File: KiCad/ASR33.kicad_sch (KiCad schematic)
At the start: 34 parts, among them J1 USB-C, J2 Start, J3 Control, J4 Tx/Rx, U1 ESP32-WROOM-32, U2 FT231XQ, U3 NCR402U, U4 NCR402U, U5 NX6020CAKS, U6 LMR16006+FB

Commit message: Notes
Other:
- note added: "Look in to clamp diode on Rx Check all GPIO are clean Add QR code"
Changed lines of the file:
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@@
     (stroke (width 0) (type default) (color 0 0 0 0))
+  )
+  (text "Look in to clamp diode on Rx\nCheck all GPIO are clean\nAdd QR code"
+    (at 29.845 127.635 0)
+    (effects (font (size 10 10) (thickness 2) bold) (justify left bottom))
   )
   (global_label "MOTOR" (shape input) (at 127 113.03 180) (fields_autoplaced)

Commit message: Reworked
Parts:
- removed J2: Start, RevK:Molex_MiniSPOX_H2RA, symbol Connector_Generic:Conn_01x02
- removed J3: Control, RevK:Molex_MiniSPOX_H3RA, symbol Connector_Generic:Conn_01x03
- removed J4: Tx/Rx, RevK:Molex_MiniSPOX_H4RA, symbol Connector_Generic:Conn_01x04
- removed R9: 10K, RevK:R_0603, symbol Device:R
- removed U5: NX6020CAKS, Package_TO_SOT_SMD:SOT-363_SC-70-6, symbol RevK:NX6020CAKS
- added C5: NF, RevK:C_0603, symbol Device:C
- added J2: Control, RevK:Molex_MiniSPOX_H3RA, symbol Connector_Generic:Conn_01x03
- added J3: Teletype, RevK:Molex_MiniSPOX_H6RA, symbol Connector_Generic:Conn_01x06
- added Q1: NX7002AK, Package_TO_SOT_SMD:SOT-23, symbol RevK:NX7002AK
- added U6: QR, RevK:QR-ASR33, symbol RevK:QR
- renumbered C5 to C6, C6 to C7, C7 to C8, R11 to R9, U6 to U5
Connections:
- net CHARGER: now also U1.24 (IO2); no longer U1.29 (IO5)
- net GND: now also C5.1, J2.1 (Pin_1), J3.1 (Pin_1), Q1.2 (S)
- net MOTOR: now also D2.6 (K3A4), U1.37 (IO23), J2.3 (Pin_3); no longer D2.3 (K1A2), U1.30 (IO18)
- net POWER: now also D2.3 (K1A2), U1.36 (IO22), J2.2 (Pin_2); no longer D2.6 (K3A4), U1.31 (IO19)
- net RX20MA: now also D3.6 (K3A4), U1.28 (IO17), C5.2, J3.6 (Pin_6); no longer D3.3 (K1A2), U1.27 (IO16)
- net START: now also D3.3 (K1A2), U1.26 (IO4), J3.2 (Pin_2); no longer D3.6 (K3A4), U1.37 (IO23)
- net TX20MA: now also U1.27 (IO16), Q1.1 (G); no longer U1.26 (IO4)
- net USB: now also U1.23 (IO15); no longer U1.28 (IO17)
- net at U3.2 (IOUT), U3.3 (IOUT), U3.5 (IOUT): now also J3.3 (Pin_3)
- net at U4.2 (IOUT), U4.3 (IOUT), U4.5 (IOUT): now also J3.5 (Pin_5)
- new net: J3.4 (Pin_4), Q1.3 (D)
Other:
- note removed: "Look in to clamp diode on Rx Check all GPIO are clean Add QR code"
- moved on the sheet: R9

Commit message: New PCB
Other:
- note added: "Maybe button for AP mode?"
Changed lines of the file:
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@@
     (stroke (width 0) (type default) (color 0 0 0 0))
+  )
+  (text "Maybe button for AP mode?" (at 34.925 23.495 0)
+    (effects (font (size 10 10) (thickness 2) bold) (justify left bottom))
   )
   (global_label "MOTOR" (shape input) (at 127 97.79 180) (fields_autoplaced)

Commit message: Tweak, added button
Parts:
- added SW1: SW_Push, RevK:SW_PUSH_6mm_PTH, symbol Switch:SW_Push
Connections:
- net GND: now also SW1.1
- net BUTTON: now reaches U1.16 (IO13)
- net BUTTON: now also SW1.2
- no-connect marks 25 -> 24
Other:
- note removed: "Maybe button for AP mode?"

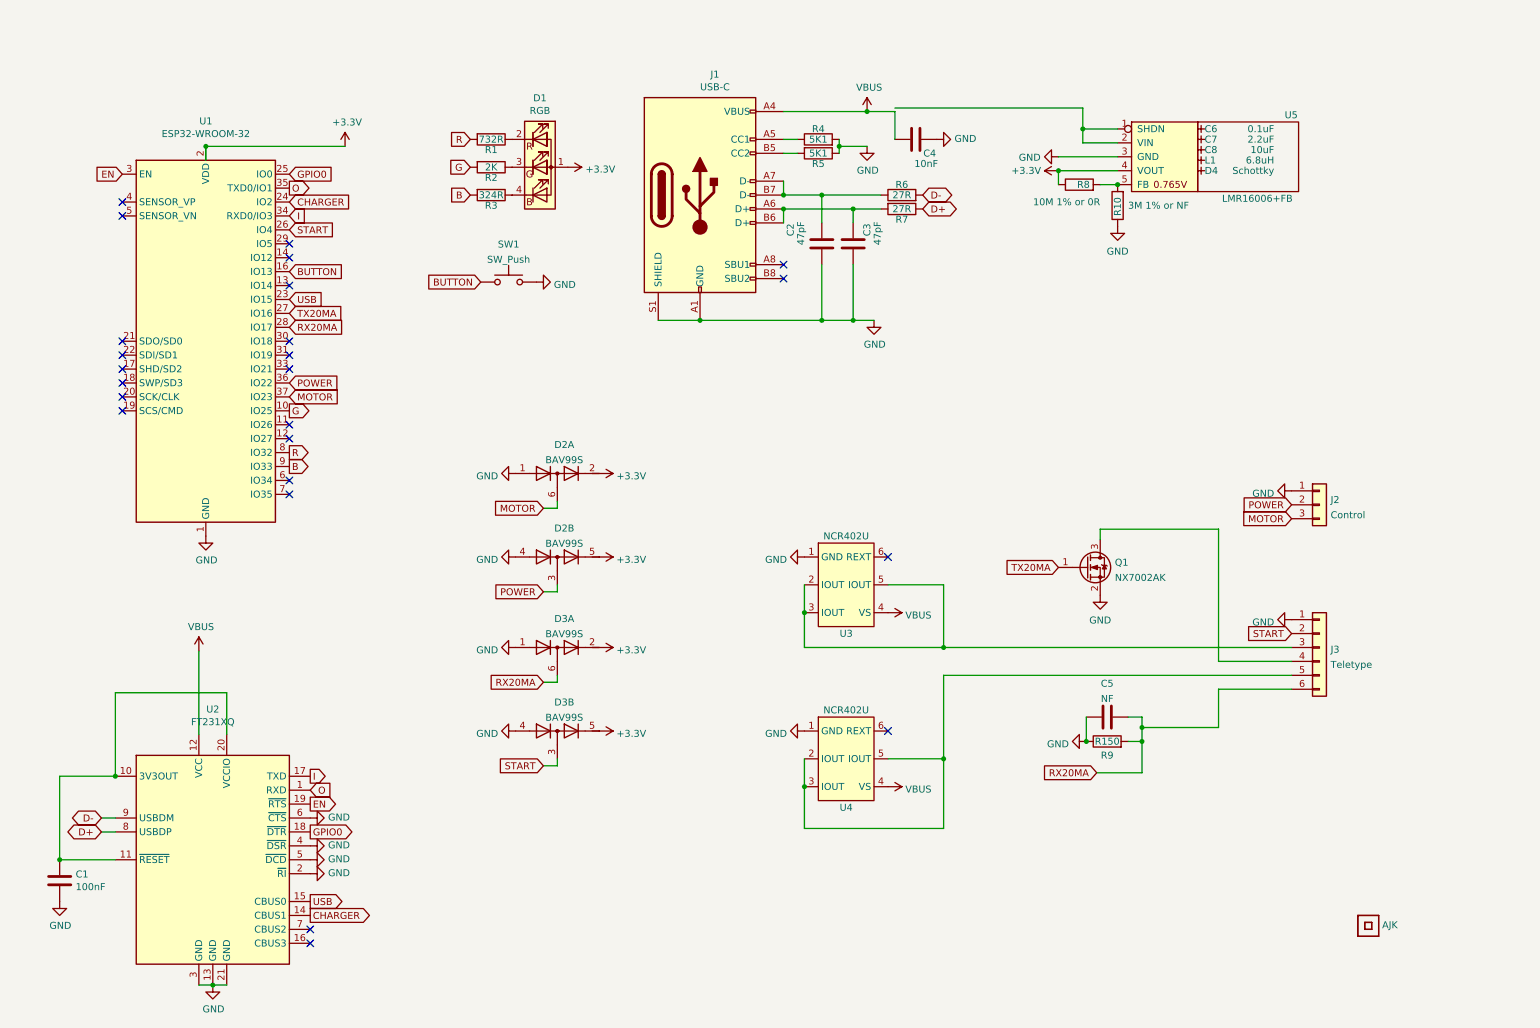
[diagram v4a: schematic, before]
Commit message: Reworkd tx/rx
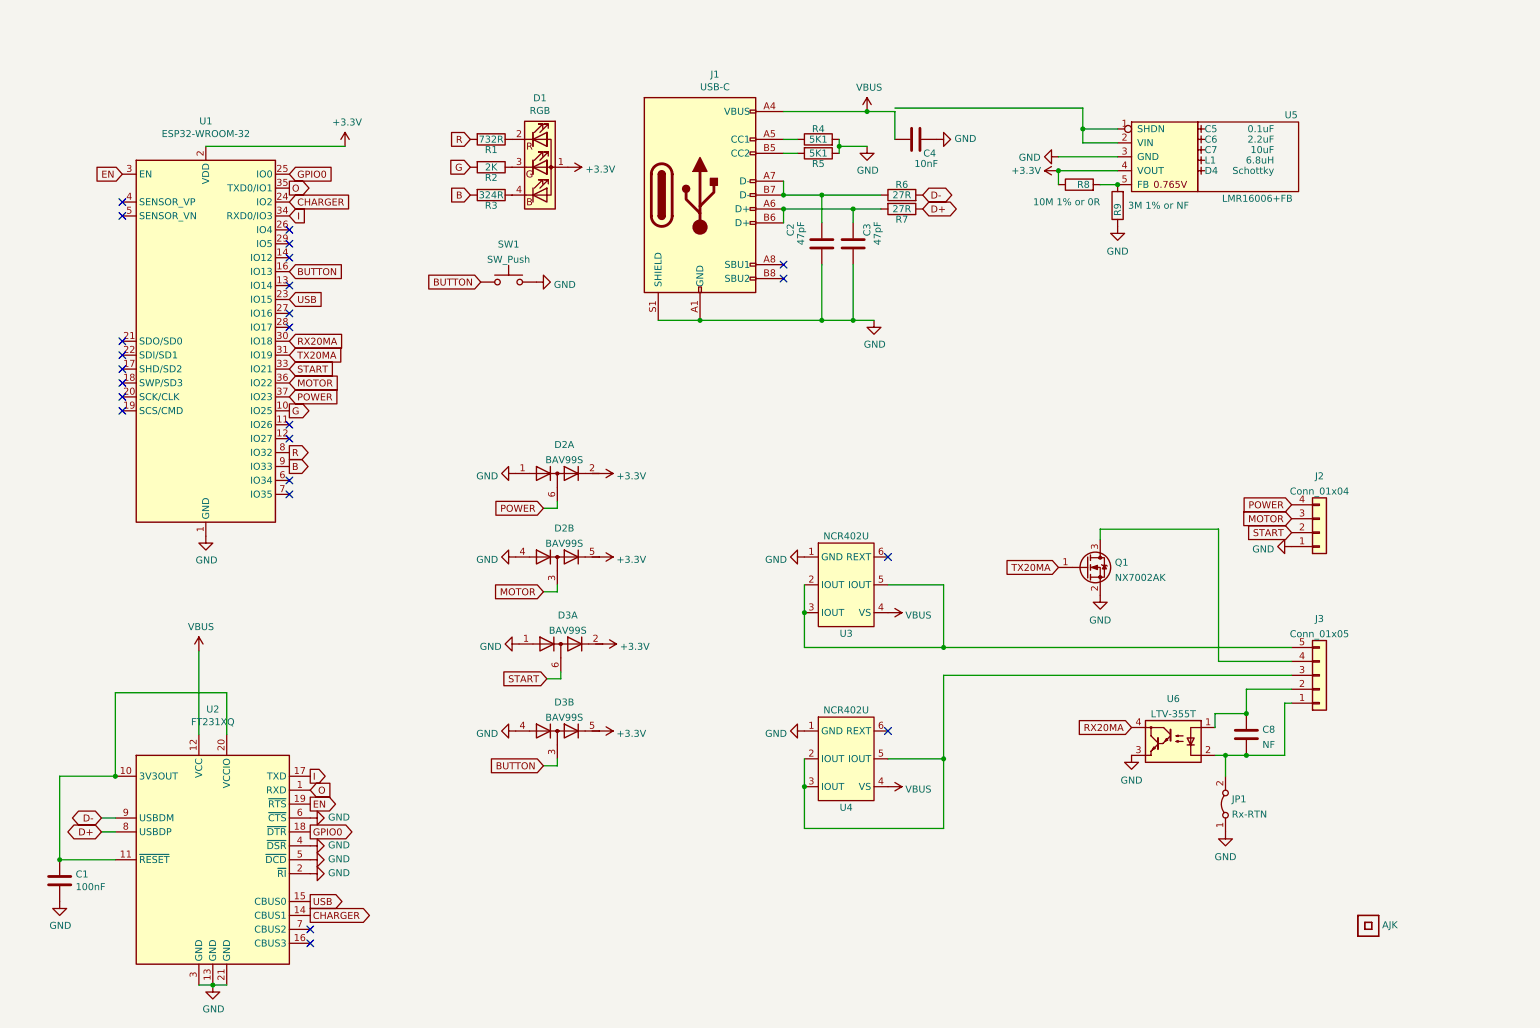
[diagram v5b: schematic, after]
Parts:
- removed J2: Control, RevK:Molex_MiniSPOX_H3RA, symbol Connector_Generic:Conn_01x03
- removed J3: Teletype, RevK:Molex_MiniSPOX_H6RA, symbol Connector_Generic:Conn_01x06
- removed R9: R150, RevK:R_0603, symbol Device:R
- added J2: Conn_01x04, RevK:Molex_MiniSPOX_H4RA, symbol Connector_Generic:Conn_01x04
- added J3: Conn_01x05, RevK:Molex_MiniSPOX_H5RA, symbol Connector_Generic:Conn_01x05
- added JP1: Rx-RTN, Jumper:SolderJumper-2_P1.3mm_Bridged2Bar_RoundedPad1.0x1.5mm, symbol Jumper:Jumper_2_Bridged
- added U6: LTV-355T, Package_SO:SO-4_4.4x3.6mm_P2.54mm, symbol Isolator:LTV-355T
- renumbered C6 to C5, C7 to C6, C8 to C7, C5 to C8, R10 to R9, U6 to U7
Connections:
- net BUTTON: now also D3.3 (K1A2)
- net GND: now also J2.1 (Pin_1), JP1.1 (A), U6.3; no longer C8.1
- net MOTOR: now also D2.3 (K1A2), U1.36 (IO22), J2.3 (Pin_3); no longer D2.6 (K3A4), U1.37 (IO23)
- net POWER: now also D2.6 (K3A4), U1.37 (IO23), J2.4 (Pin_4); no longer D2.3 (K1A2), U1.36 (IO22)
- net RX20MA: now also U1.30 (IO18), U6.4; no longer C8.2, D3.6 (K3A4), U1.28 (IO17)
- net START: now also D3.6 (K3A4), U1.33 (IO21), J2.2 (Pin_2); no longer D3.3 (K1A2), U1.26 (IO4)
- net TX20MA: now also U1.31 (IO19); no longer U1.27 (IO16)
- net at Q1.3 (D): now also J3.4 (Pin_4)
- net at U3.2 (IOUT), U3.3 (IOUT), U3.5 (IOUT): now also J3.5 (Pin_5)
- net at U4.2 (IOUT), U4.3 (IOUT), U4.5 (IOUT): now also J3.3 (Pin_3)
- new net: C8.1, J3.1 (Pin_1), JP1.2 (B), U6.2
- new net: C8.2, J3.2 (Pin_2), U6.1
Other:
- moved on the sheet: C8

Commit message: Reworked PCB and manuals
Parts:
- JP1: footprint Jumper:SolderJumper-2_P1.3mm_Bridged2Bar_RoundedPad1.0x1.5mm -> RevK:SolderJumper-2_P1.3mm_Bridged2Bar_RoundedPad1.0x1.5mm
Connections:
- net MOTOR renamed MTR
- net POWER renamed PWR
- net START renamed RUN
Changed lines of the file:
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@@
     (stroke (width 0) (type default) (color 0 0 0 0))
   )
-  (global_label "MOTOR" (shape input) (at 127 113.03 180) (fields_autoplaced)
+  (global_label "MTR" (shape input) (at 127 113.03 180) (fields_autoplaced)
     (effects (font (size 1.27 1.27)) (justify right))
-    (property "Intersheet References" "${INTERSHEET_REFS}" (id 0) (at 118.3258 112.9506 0)
+    (property "Intersheet References" "${INTERSHEET_REFS}" (id 0) (at 120.9868 112.9506 0)
       (effects (font (size 1.27 1.27)) (justify right) hide)
     )
@@
     )
   )
-  (global_label "START" (shape input) (at 127.635 128.905 180) (fields_autoplaced)
+  (global_label "RUN" (shape input) (at 127.635 128.905 180) (fields_autoplaced)
     (effects (font (size 1.27 1.27)) (justify right))
-    (property "Intersheet References" "${INTERSHEET_REFS}" (id 0) (at 119.8075 128.8256 0)
+    (property "Intersheet References" "${INTERSHEET_REFS}" (id 0) (at 121.3798 128.8256 0)
       (effects (font (size 1.27 1.27)) (justify right) hide)
     )
@@
     )
   )
-  (global_label "START" (shape input) (at 263.525 102.235 180) (fields_autoplaced)
+  (global_label "RUN" (shape input) (at 263.525 102.235 180) (fields_autoplaced)
     (effects (font (size 1.27 1.27)) (justify right))
-    (property "Intersheet References" "${INTERSHEET_REFS}" (id 0) (at 255.6975 102.1556 0)
+    (property "Intersheet References" "${INTERSHEET_REFS}" (id 0) (at 257.2698 102.1556 0)
       (effects (font (size 1.27 1.27)) (justify right) hide)
     )
@@
     )
   )
-  (global_label "POWER" (shape input) (at 263.525 97.155 180) (fields_autoplaced)
+  (global_label "PWR" (shape input) (at 263.525 97.155 180) (fields_autoplaced)
     (effects (font (size 1.27 1.27)) (justify right))
-    (property "Intersheet References" "${INTERSHEET_REFS}" (id 0) (at 254.7298 97.0756 0)
+    (property "Intersheet References" "${INTERSHEET_REFS}" (id 0) (at 257.2094 97.0756 0)
       (effects (font (size 1.27 1.27)) (justify right) hide)
     )
@@
     )
   )
-  (global_label "MOTOR" (shape input) (at 80.645 74.93 0) (fields_autoplaced)
-    (effects (font (size 1.27 1.27)) (justify left))
-    (property "Intersheet References" "${INTERSHEET_REFS}" (id 0) (at 89.3192 74.8506 0)
+  (global_label "MTR" (shape input) (at 80.645 74.93 0) (fields_autoplaced)
+    (effects (font (size 1.27 1.27)) (justify left))
+    (property "Intersheet References" "${INTERSHEET_REFS}" (id 0) (at 86.6582 74.8506 0)
       (effects (font (size 1.27 1.27)) (justify left) hide)
     )
@@
     )
   )
-  (global_label "POWER" (shape input) (at 80.645 77.47 0) (fields_autoplaced)
-    (effects (font (size 1.27 1.27)) (justify left))
-    (property "Intersheet References" "${INTERSHEET_REFS}" (id 0) (at 89.4402 77.3906 0)
+  (global_label "PWR" (shape input) (at 80.645 77.47 0) (fields_autoplaced)
+    (effects (font (size 1.27 1.27)) (justify left))
+    (property "Intersheet References" "${INTERSHEET_REFS}" (id 0) (at 86.9606 77.3906 0)
       (effects (font (size 1.27 1.27)) (justify left) hide)
     )
@@
     )
   )
-  (global_label "POWER" (shape input) (at 127 97.79 180) (fields_autoplaced)
+  (global_label "PWR" (shape input) (at 127 97.79 180) (fields_autoplaced)
     (effects (font (size 1.27 1.27)) (justify right))
-    (property "Intersheet References" "${INTERSHEET_REFS}" (id 0) (at 118.2048 97.7106 0)
+    (property "Intersheet References" "${INTERSHEET_REFS}" (id 0) (at 120.6844 97.7106 0)
       (effects (font (size 1.27 1.27)) (justify right) hide)
     )
@@
     )
   )
-  (global_label "MOTOR" (shape input) (at 263.525 99.695 180) (fields_autoplaced)
+  (global_label "MTR" (shape input) (at 263.525 99.695 180) (fields_autoplaced)
     (effects (font (size 1.27 1.27)) (justify right))
-    (property "Intersheet References" "${INTERSHEET_REFS}" (id 0) (at 254.8508 99.6156 0)
+    (property "Intersheet References" "${INTERSHEET_REFS}" (id 0) (at 257.5118 99.6156 0)
       (effects (font (size 1.27 1.27)) (justify right) hide)
     )
@@
     )
   )
-  (global_label "START" (shape input) (at 80.645 72.39 0) (fields_autoplaced)
-    (effects (font (size 1.27 1.27)) (justify left))
-    (property "Intersheet References" "${INTERSHEET_REFS}" (id 0) (at 88.4725 72.3106 0)
+  (global_label "RUN" (shape input) (at 80.645 72.39 0) (fields_autoplaced)
+    (effects (font (size 1.27 1.27)) (justify left))
+    (property "Intersheet References" "${INTERSHEET_REFS}" (id 0) (at 86.9002 72.3106 0)
       (effects (font (size 1.27 1.27)) (justify left) hide)
     )
@@
       (effects (font (size 1.27 1.27)) (justify right))
     )
-    (property "Footprint" "Jumper:SolderJumper-2_P1.3mm_Bridged2Bar_RoundedPad1.0x1.5mm" (id 2) (at 251.46 151.765 0)
+    (property "Footprint" "RevK:SolderJumper-2_P1.3mm_Bridged2Bar_RoundedPad1.0x1.5mm" (id 2) (at 251.46 151.765 0)
       (effects (font (size 1.27 1.27)) hide)
     )
@@
     )
     (path "/79f55ec2-8220-4514-8d65-f6c3a7138618"
-      (reference "JP1") (unit 1) (value "Rx-RTN") (footprint "Jumper:SolderJumper-2_P1.3mm_Bridged2Bar_RoundedPad1.0x1.5mm")
+      (reference "JP1") (unit 1) (value "Rx-RTN") (footprint "RevK:SolderJumper-2_P1.3mm_Bridged2Bar_RoundedPad1.0x1.5mm")
     )
     (path "/00000000-0000-0000-0000-0000610fe01a"

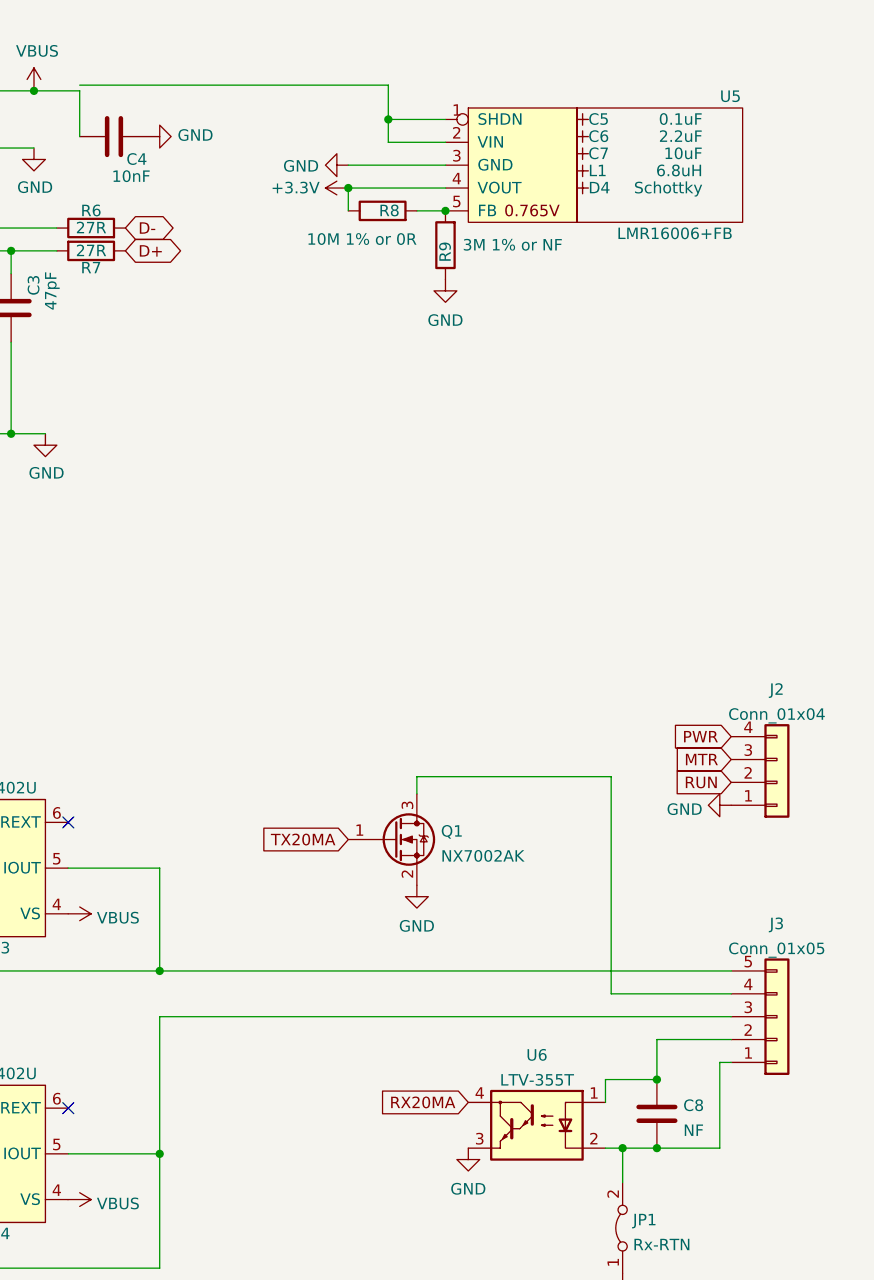
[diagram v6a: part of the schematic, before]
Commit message: Added network on Tx, same as FS-2 send circuit.
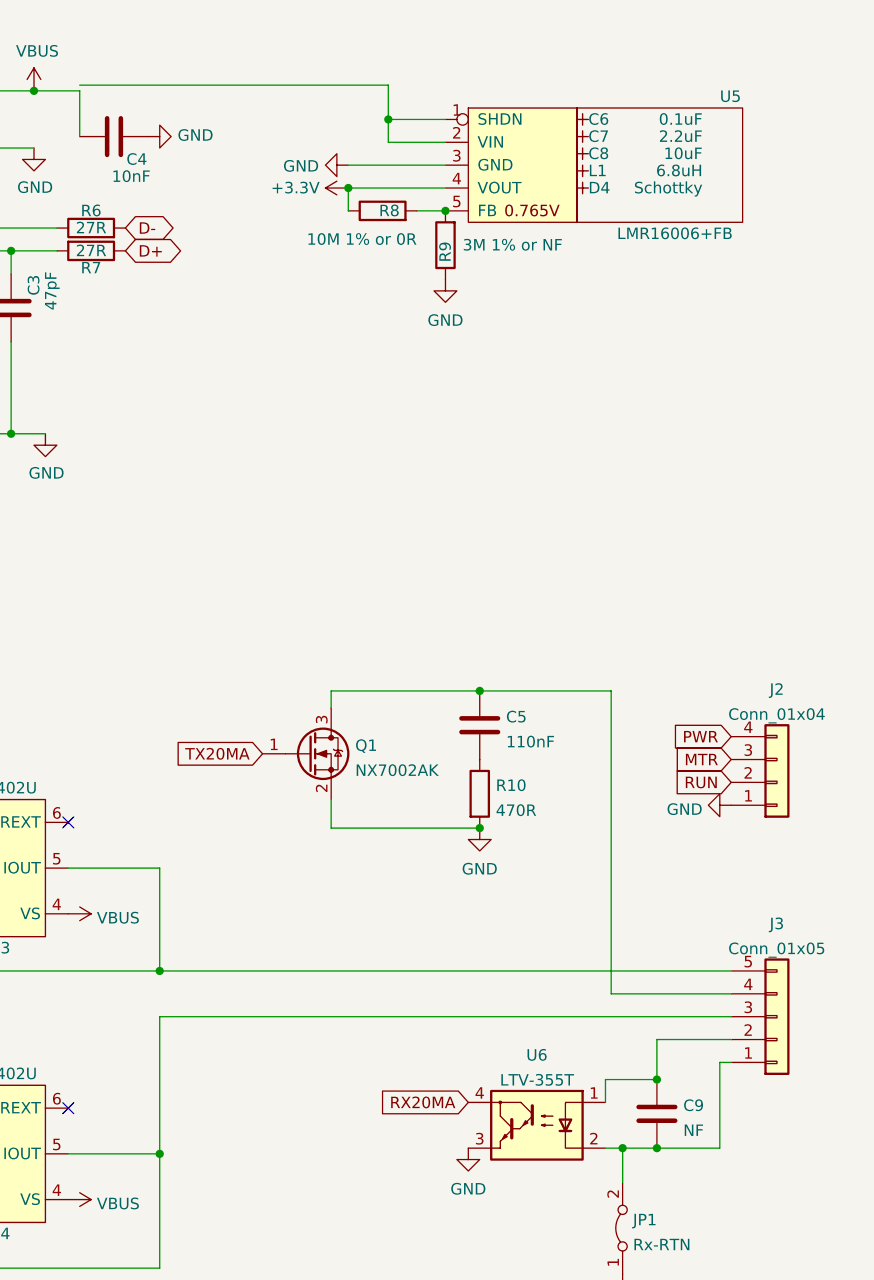
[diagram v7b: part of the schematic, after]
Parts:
- added C5: 110nF, Capacitor_SMD:C_1206_3216Metric, symbol Device:C
- added R10: 470R, RevK:R_0603, symbol Device:R
- renumbered C5 to C6, C6 to C7, C7 to C8, C8 to C9
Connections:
- net GND: now also R10.2
- net at J3.4 (Pin_4), Q1.3 (D): now also C5.1
- new net: C5.2, R10.1
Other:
- moved on the sheet: Q1
